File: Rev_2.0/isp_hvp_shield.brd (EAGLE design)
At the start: 50 x 53 mm, 26 parts, among them IC1 ATtiny13/15/25/45/85, IC2 ATtiny24/44/84, IC3 TINY26/261/461/861, IC4 ATtiny2313/4313, IC5 ATMEGA328, IC6 74HCT595D, IC7 MAX662A, Q1 BC858BSMD

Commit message: More cleaning...
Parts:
- removed U$1: (no value), kaibader:OSHW-LOGO-S
- removed U$3: (no value), kaibader:KAI-LOGO-M
- added E$1: (no value), kaibader:KAI-LOGO-M
- added E$2: (no value), kaibader:OSHW-LOGO-S
- PINS: value UNO_R3_SHIELDV1 -> (none)
- moved PINS 0.08 mm to (-7.65, 53.0)
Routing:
- net Q4: track 91.6 -> 60.6 mm, vias 1 -> 0
- net VCC: track 77.6 -> 47.6 mm, vias 0 -> 2
- net A4: track 117.6 -> 94.5 mm, vias 1 -> 0
- net D11_MOSI: track 102.4 -> 80.4 mm, vias 2 -> 1
- net Q0: track 92.9 -> 77.1 mm, vias 2 -> 0
- net +5V: track 103.3 -> 88.1 mm, vias 0 -> 1
- net D2: track 44.4 -> 34.2 mm
- net D3: track 39.0 -> 29.8 mm, vias 2 -> 0
- net N$1: track 27.7 -> 18.8 mm
- net D10_RESET: track 93.3 -> 85.0 mm
- net D10: track 61.3 -> 53.2 mm, vias 1 -> 2
- net A2_SER: track 16.7 -> 9.73 mm
- net Q3: track 74.9 -> 69.2 mm, vias 2 -> 1
- net D4: track 32.4 -> 26.8 mm, vias 2 -> 0
- net A1_RCK: track 13.5 -> 9.73 mm
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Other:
- board text added: "Kai C. Bader CC-BY-SA 3.0"
- board text removed: "CC-BY-SA 3.0"
- board text removed: "Kai C. Bader"

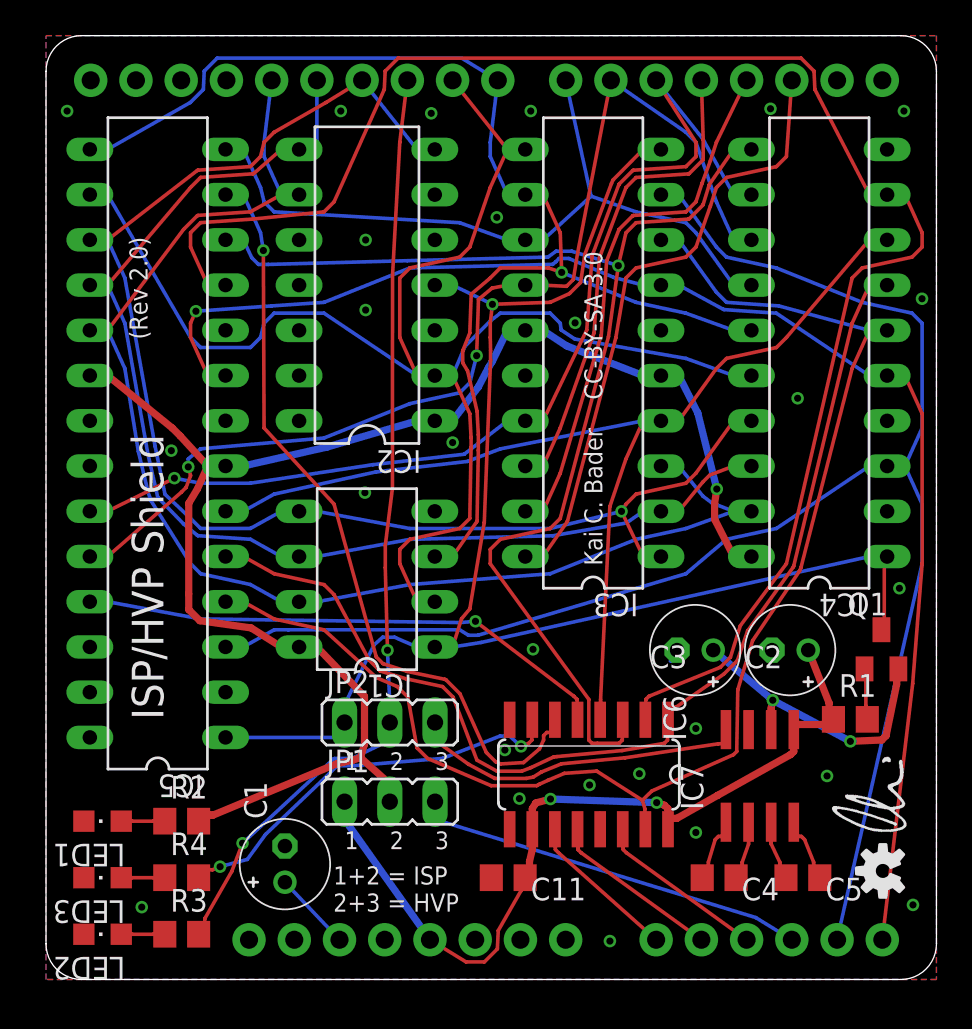
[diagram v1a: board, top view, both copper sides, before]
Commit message: Fixed the forward<->backward compatibility.
- Ripped up the board file to fix the schematic board compatibility.
- Moved the TopoR (auto)routed board to a different location.
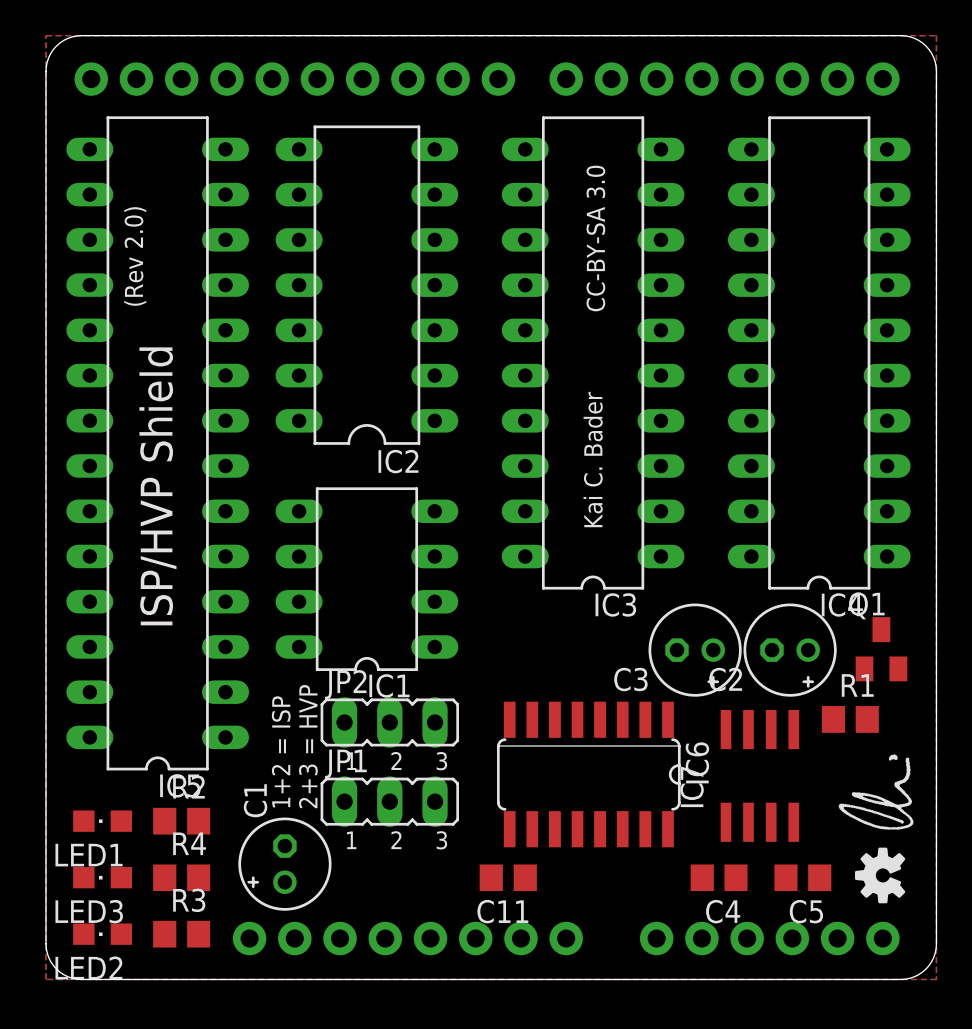
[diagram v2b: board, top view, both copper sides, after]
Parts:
- removed E$1: (no value), kaibader:KAI-LOGO-M
- removed E$2: (no value), kaibader:OSHW-LOGO-S
- added U$1: (no value), kaibader:OSHW-LOGO-S
- added U$3: (no value), kaibader:KAI-LOGO-M
- PINS: value (none) -> UNO_R3_SHIELDV1
- moved PINS 0.08 mm to (-7.62, 53.1)
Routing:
- net A4: track 94.5 -> 0.00 mm
- net Q2: track 91.8 -> 0.00 mm
- net +5V: track 88.1 -> 0.00 mm, vias 1 -> 0
- net D9: track 87.8 -> 0.00 mm
- net D10_RESET: track 85.0 -> 0.00 mm, vias 1 -> 0
- net D11_MOSI: track 80.4 -> 0.00 mm, vias 1 -> 0
- net A5: track 78.9 -> 0.00 mm, vias 1 -> 0
- net Q0: track 77.1 -> 0.00 mm
- net D13_SCK: track 75.8 -> 0.00 mm
- net D8: track 72.1 -> 0.00 mm, vias 1 -> 0
- net Q3: track 69.2 -> 0.00 mm, vias 1 -> 0
- net D12_MISO: track 69.1 -> 0.00 mm
- net Q1: track 61.1 -> 0.00 mm
- net Q4: track 60.6 -> 0.00 mm
- net D6: track 59.9 -> 0.00 mm, vias 2 -> 0
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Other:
- board text added: "CC-BY-SA 3.0"
- board text added: "Kai C. Bader"
- board text removed: "Kai C. Bader CC-BY-SA 3.0"
